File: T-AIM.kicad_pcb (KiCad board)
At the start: 2 copper layers, 44 parts, among them IC1 ATMEGA328PB-A, IC2 MAX17043, J1 ADXL345 Connector, J2 PIR Sensor Connector, J3 JY-MCU HC-05 Pins, SW1 Connection Button, SW2 Reset Button, U1 TPS61200

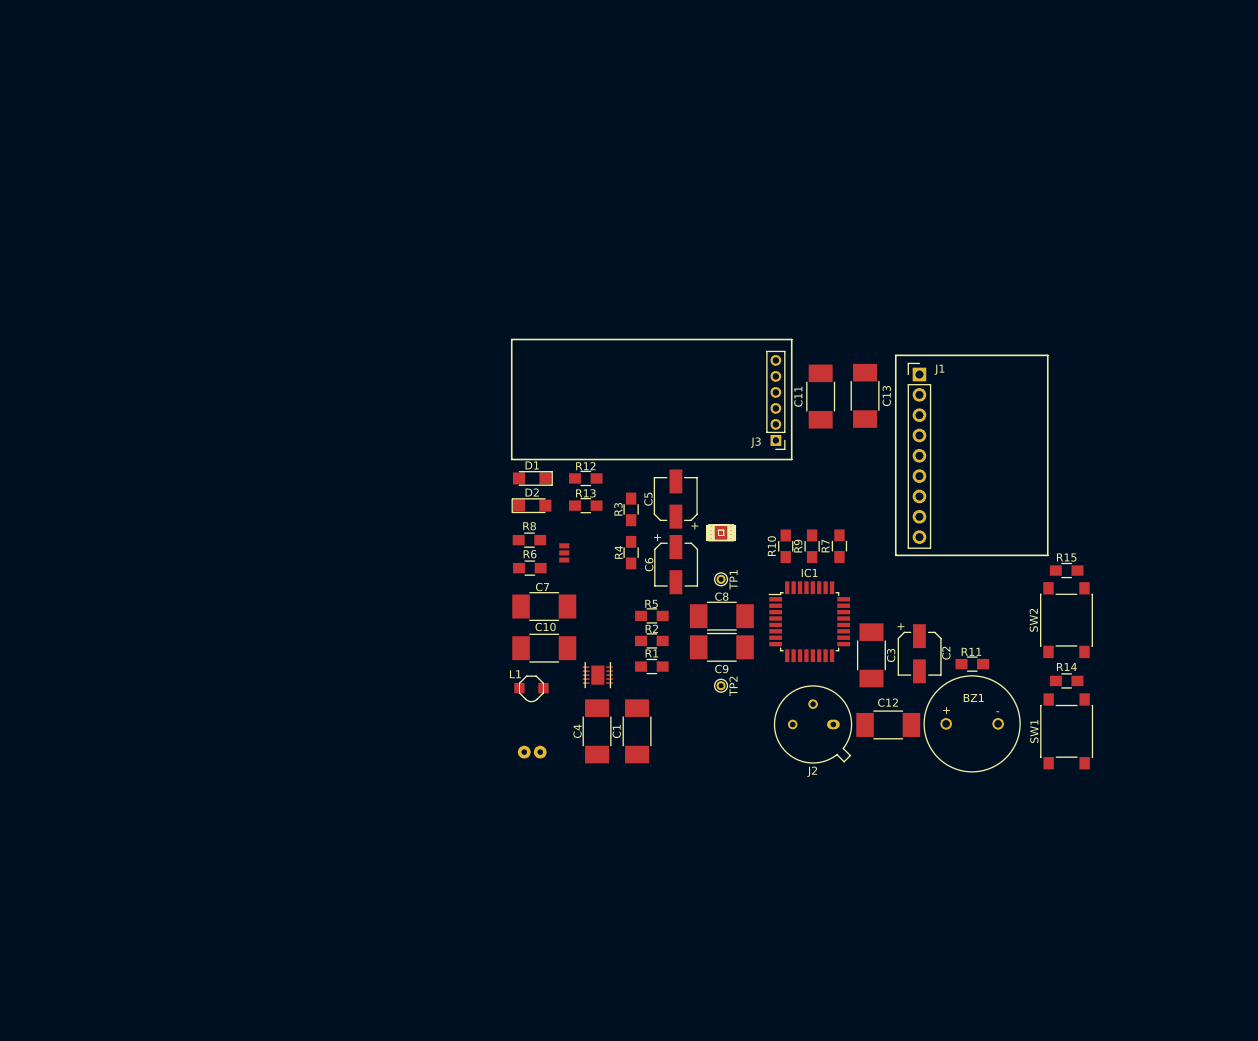
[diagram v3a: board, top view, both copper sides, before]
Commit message: First complete layout
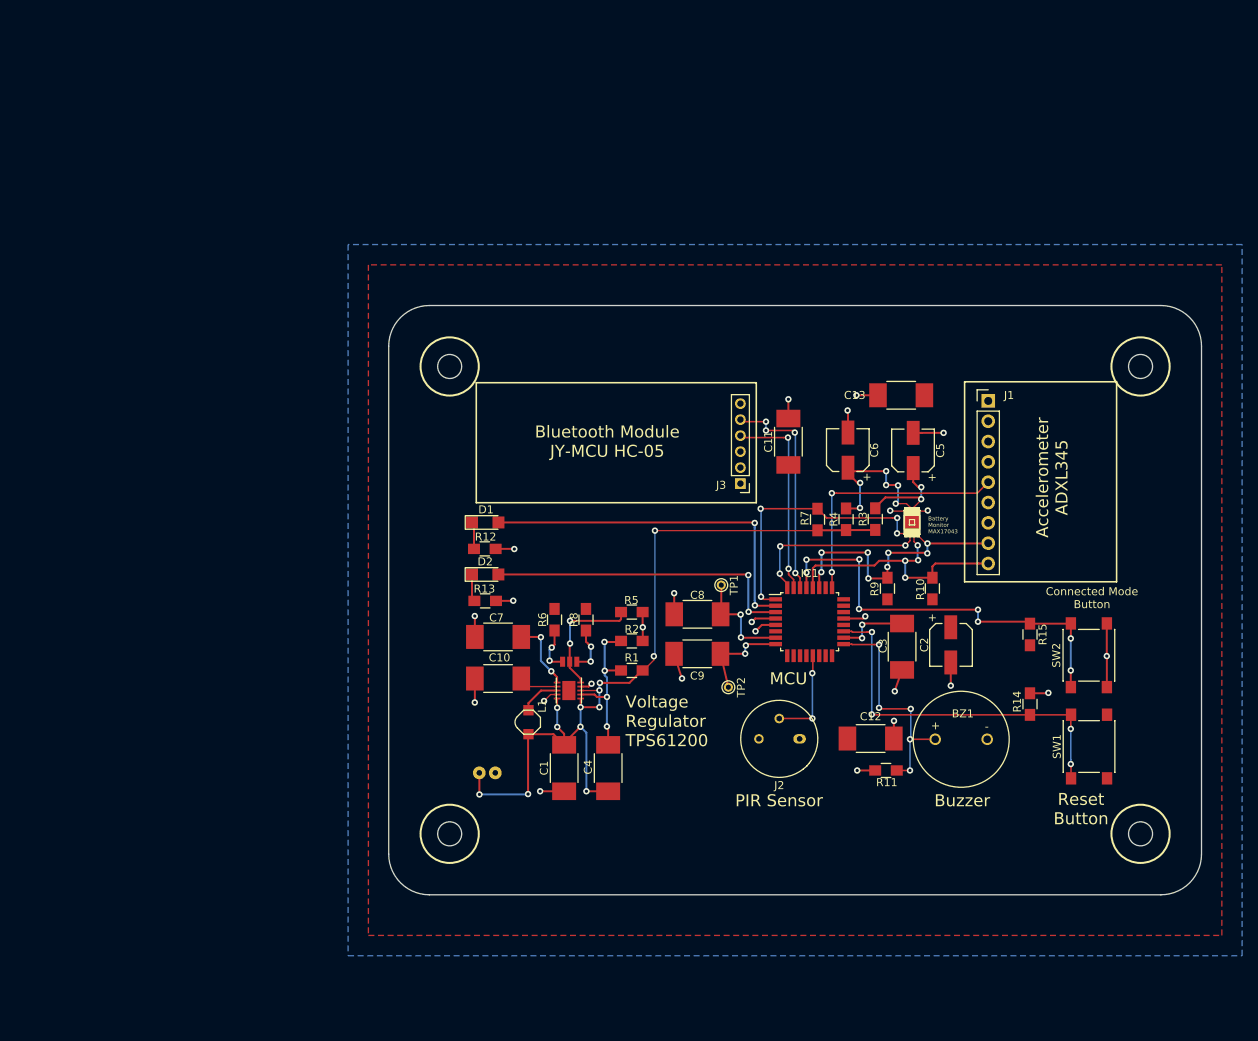
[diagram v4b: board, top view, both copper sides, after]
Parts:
- added ?: Screw_Hole_3_mm, T-AIM:Screw_Hole_3_mm, F.Cu at (118.9, 119.7)
- added ?: Screw_Hole_3_mm, T-AIM:Screw_Hole_3_mm, F.Cu at (205.3, 119.7)
- added ?: Screw_Hole_3_mm, T-AIM:Screw_Hole_3_mm, F.Cu at (205.3, 61.2)
- added ?: Screw_Hole_3_mm, T-AIM:Screw_Hole_3_mm, F.Cu at (118.9, 61.2)
- J2: footprint TO_SOT_Packages_THT:TO-5-3 -> T-AIM:TO-5-3
- moved R3 30.5 mm to (172.1, 80.3), turned to 90 degrees
- moved C5 30.3 mm to (176.8, 71.7)
- moved R4 27.2 mm to (168.5, 80.3), turned to 90 degrees
- moved C6 25.8 mm to (168.7, 71.7), turned to 90 degrees
- moved IC2 23.9 mm to (176.7, 80.7), turned to 270 degrees
- moved R10 19.1 mm to (179.2, 89.0)
- moved R13 17.3 mm to (123.3, 90.5)
- moved R11 17.1 mm to (173.4, 111.7), turned to 0 degrees
- moved R12 15.4 mm to (123.3, 84.0)
- moved SJ1 13.6 mm to (133.9, 98.2), turned to 0 degrees
- moved R8 12.2 mm to (135.9, 92.9), turned to 270 degrees
- moved R9 10.8 mm to (173.6, 89.0)
- moved D2 10.4 mm to (123.3, 87.2)
- moved C1 10.2 mm to (133.2, 111.4)
- moved R15 9.21 mm to (191.4, 94.7), turned to 90 degrees
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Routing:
- net VCC: track 0.00 -> 108.2 mm, vias 0 -> 12
- net GND: track 0.00 -> 67.2 mm, vias 0 -> 24
- net ResetButton: track 0.00 -> 52.5 mm, vias 0 -> 8
- net ConnectedButton: track 0.00 -> 46.8 mm, vias 0 -> 4
- net RedLED: track 0.00 -> 45.0 mm, vias 0 -> 2
- net BlueLED: track 0.00 -> 39.3 mm, vias 0 -> 2
- net /SDA: track 0.00 -> 34.8 mm, vias 0 -> 8
- net /SCL: track 0.00 -> 33.7 mm, vias 0 -> 4
- net BatteryLowAlert: track 0.00 -> 32.6 mm, vias 0 -> 4
- net INT1: track 0.00 -> 32.0 mm, vias 0 -> 2
- net AlarmBuzzer: track 0.00 -> 28.9 mm, vias 0 -> 5
- net BL_RXD: track 0.00 -> 27.8 mm, vias 0 -> 4
- net BL_TXD: track 0.00 -> 25.1 mm, vias 0 -> 2
- net FuelGaugeRestart: track 0.00 -> 23.0 mm, vias 0 -> 3
- net Net-(C6-Pad1): track 0.00 -> 21.3 mm, vias 0 -> 6
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- added copper zone on F.Cu, net 3V3
- added copper zone on B.Cu, net GND
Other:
- board outline added: 101.6 x 73.7 mm
- net class Power: clearance 0.2 -> 0.25; trace_width 0.2 -> 0.25
- net class Signal: clearance 0.1 -> 0.2; trace_width 0.1 -> 0.2
- board text added: "Accelerometer ADXL345"
- board text added: "Battery Monitor MAX17043"
- board text added: "Bluetooth Module JY-MCU HC-05"
- board text added: "Buzzer"
- board text added: "Connected Mode Button"
- board text added: "MCU"
- board text added: "PIR Sensor"
- board text added: "Reset Button"
- board text added: "Voltage Regulator TPS61200"

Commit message: Schematic updated for 3.7V; Changed Buzzer resistor to 1M; PCB updated for SF LiPo Gauge; Gerbers generated
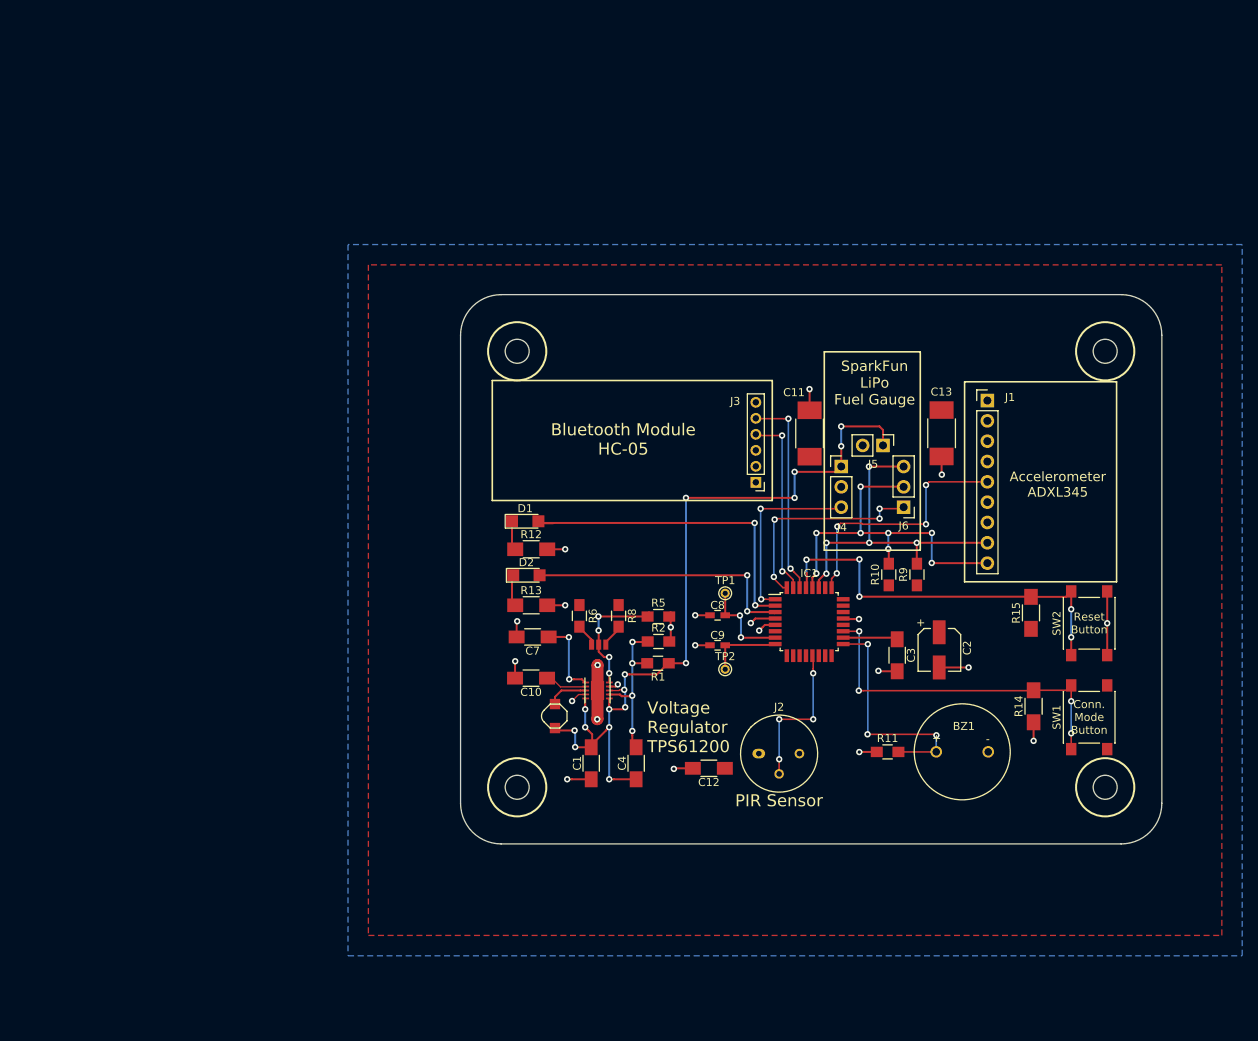
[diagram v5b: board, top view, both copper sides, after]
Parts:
- removed ? (x4): Screw_Hole_3_mm, T-AIM:Screw_Hole_3_mm
- removed C5: 1uF, Capacitors_SMD:CP_Elec_5x5.3
- removed C6: 10nF, Capacitors_SMD:CP_Elec_5x5.3
- removed IC2: MAX17043, SparkFun-PowerIC:TDFN-8
- removed JP1: M02JST-PTH-2, SparkFun-Connectors:JST-2-PTH
- removed R3: 1k, Resistors_SMD:R_0805_HandSoldering
- removed R4: 150, Resistors_SMD:R_0805_HandSoldering
- removed R7: 4.7k, Resistors_SMD:R_0805_HandSoldering
- added J4: CONN_01X03, Pin_Headers:Pin_Header_Straight_1x03_Pitch2.54mm, F.Cu at (167.9, 73.8)
- added J5: CONN_01X02, Pin_Headers:Pin_Header_Straight_1x02_Pitch2.54mm, F.Cu at (173.1, 71.1)
- added J6: CONN_01X03, Pin_Headers:Pin_Header_Straight_1x03_Pitch2.54mm, F.Cu at (175.7, 78.8)
- added S**: Screw_Hole_3_mm, T-AIM:Screw_Hole_3_mm, F.Cu at (127.3, 59.3)
- added S**: Screw_Hole_3_mm, T-AIM:Screw_Hole_3_mm, F.Cu at (200.8, 59.3)
- added S**: Screw_Hole_3_mm, T-AIM:Screw_Hole_3_mm, F.Cu at (200.8, 113.8)
- added S**: Screw_Hole_3_mm, T-AIM:Screw_Hole_3_mm, F.Cu at (127.3, 113.8)
- C1, C10, C12, C3, C4, C7: footprint Capacitors_SMD:C_1812_HandSoldering -> Capacitors_SMD:C_1206_HandSoldering
- C8, C9: footprint Capacitors_SMD:C_1812_HandSoldering -> Capacitors_SMD:C_0603_HandSoldering
- R12, R13, R14, R15: footprint Resistors_SMD:R_0805_HandSoldering -> Resistors_SMD:R_1206_HandSoldering
- R6: value 1.2M -> 1.37M
- moved C12 20.6 mm to (151.3, 111.5), turned to 180 degrees
- moved C13 6.93 mm to (180.4, 69.6), turned to 270 degrees
- moved R12 5.80 mm to (129.1, 84.1)
- moved R13 5.78 mm to (129.1, 91.1)
- moved R10 5.72 mm to (173.8, 87.3)
- moved J2 5.42 mm to (157.5, 109.6), turned to 0 degrees
- moved D2 5.15 mm to (128.5, 87.3)
- moved D1 5.00 mm to (128.3, 80.6)
- moved C7 4.32 mm to (129.3, 95.1)
- moved SJ1 4.21 mm to (137.5, 96.0)
- moved C10 4.12 mm to (129.1, 100.2)
- moved R8 4.10 mm to (140.0, 92.4)
- moved R9 4.08 mm to (177.3, 87.3)
- moved SW2 4.00 mm to (198.8, 93.3)
- moved SW1 3.66 mm to (198.8, 105.1)
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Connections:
- net /3.3V renamed /3.6V
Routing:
- net Net-(C6-Pad1): track 21.3 -> 0.00 mm, vias 6 -> 0
- net GND: track 67.2 -> 52.3 mm, vias 24 -> 20
- net /SCL: track 33.7 -> 47.3 mm, vias 4 -> 8
- net Net-(C5-Pad1): track 13.1 -> 0.00 mm, vias 2 -> 0
- net BatteryLowAlert: track 32.6 -> 23.3 mm, vias 4 -> 2
- net /SDA: track 34.8 -> 42.8 mm, vias 8 -> 5
- net PIR_OUT: track 12.0 -> 19.0 mm, vias 2 -> 4
- net (no net): track 0.00 -> 6.80 mm, vias 0 -> 2
- net VCC: track 108.2 -> 102.0 mm, vias 12 -> 16
- net BlueLED: track 39.3 -> 34.2 mm
- net FuelGaugeRestart: track 23.0 -> 27.5 mm, vias 3 -> 4
- net RedLED: track 45.0 -> 41.6 mm
- net /5V: track 5.90 -> 2.91 mm, vias 2 -> 0
- net Net-(C9-Pad1): track 12.2 -> 9.40 mm, vias 2 -> 0
- net BL_RXD: track 27.8 -> 25.5 mm, vias 4 -> 2
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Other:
- board size 101.6 x 73.7 mm -> 87.7 x 68.7 mm
- net class EP added: clearance 0.5, trace_width 0.5, via_dia 0.8, via_drill 0.4
- board text added: "Bluetooth Module HC-05"
- board text added: "Conn. Mode Button"
- board text added: "SparkFun LiPo Fuel Gauge"
- board text added: "T-AIM Sensor Board v0.1"
- board text added: "Tenager Mekonnen & Jani Väyrynen"
- board text removed: "Battery Monitor MAX17043"
- board text removed: "Bluetooth Module JY-MCU HC-05"
- board text removed: "Buzzer"
- board text removed: "Connected Mode Button"
- board text removed: "MCU"

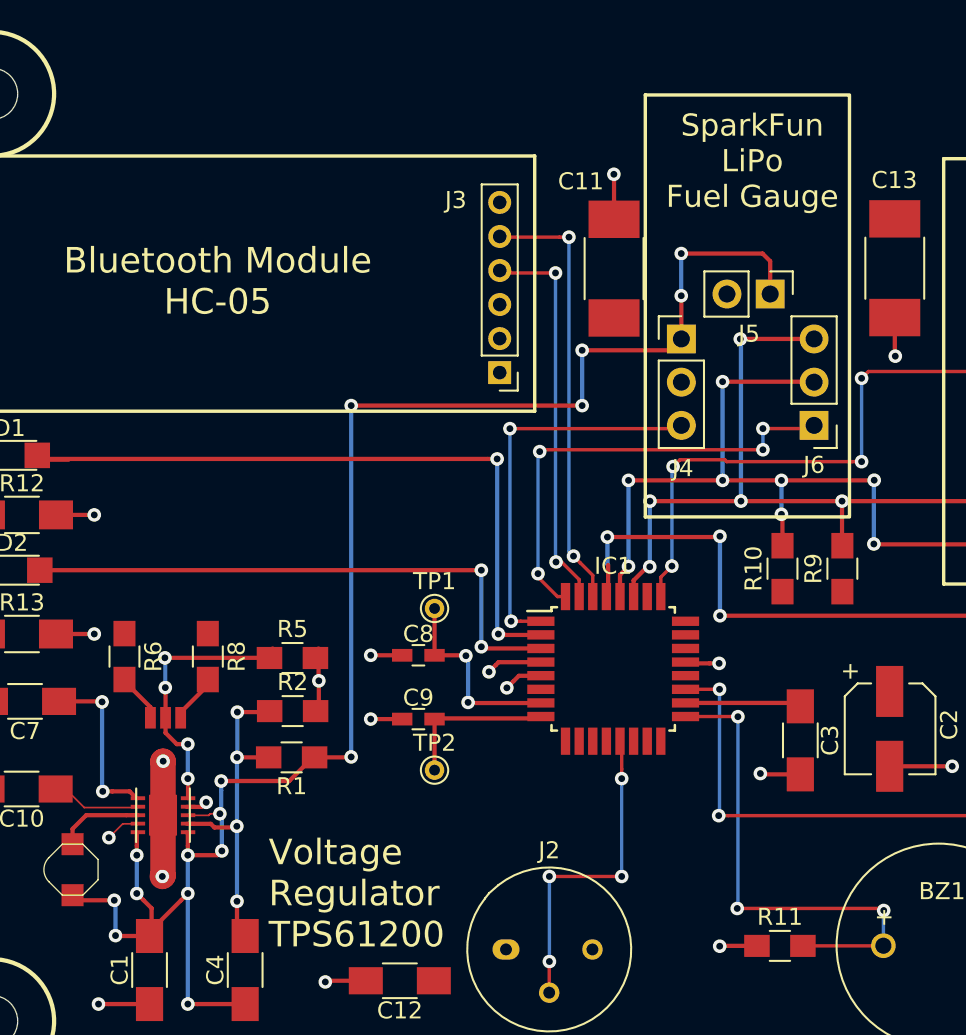
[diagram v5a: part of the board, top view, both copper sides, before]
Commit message: Updated TPS61200 Thermal Pad, PCB Layout and Gerbers; Slightly edited schematics
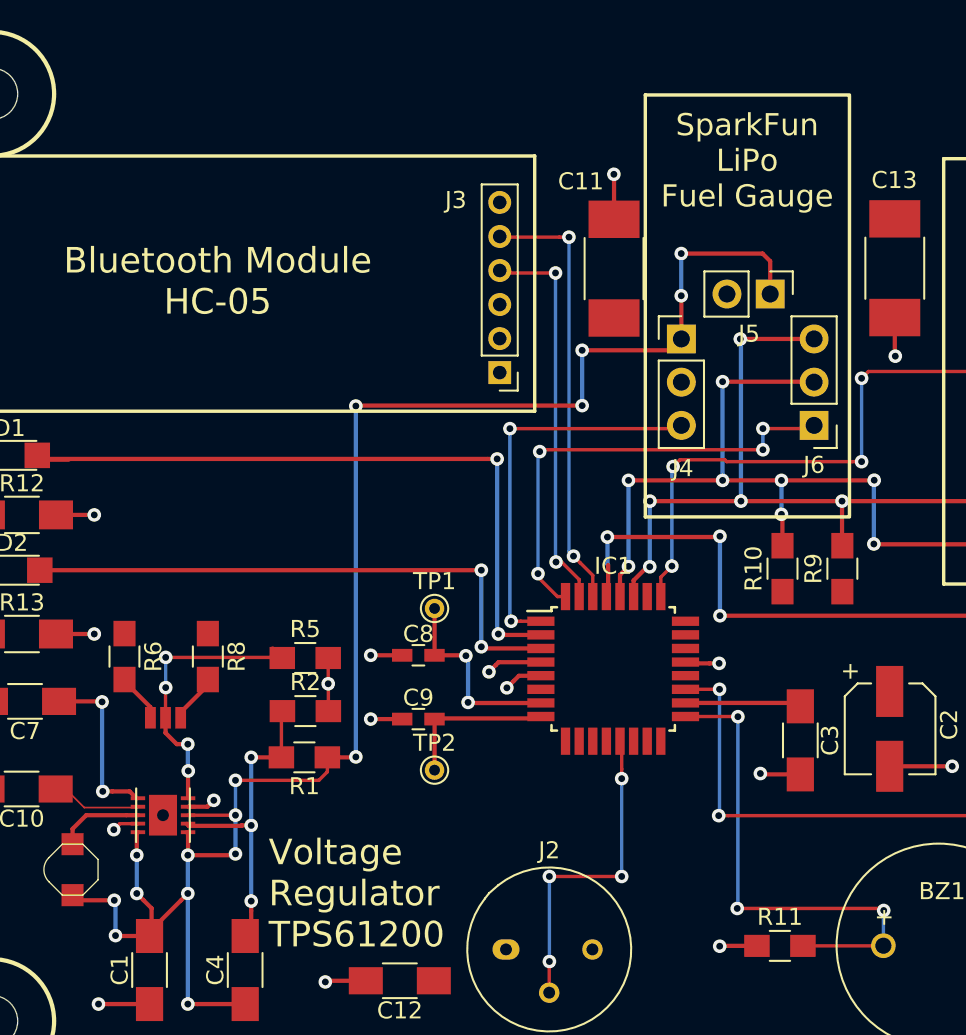
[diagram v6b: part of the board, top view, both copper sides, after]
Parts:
- R11: value 1k -> 1M
- U1: footprint SparkFun-PowerIC:DRC-10 -> DRC-10-Thermal-Vias
- moved R1 0.75 mm to (145.7, 98.3)
- moved R2 0.75 mm to (145.8, 95.6)
- moved R5 0.75 mm to (145.7, 92.5)
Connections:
- net 3V3 renamed 3V6
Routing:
- net (no net): track 6.80 -> 0.00 mm, vias 2 -> 0
- net Net-(C4-Pad2): track 20.1 -> 18.7 mm, vias 4 -> 3
- net VCC: track 102.0 -> 103.3 mm
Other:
- net class Default: clearance 0.25 -> 0.1
- net class EP: clearance 0.5 -> 0.25
- net class Power: clearance 0.25 -> 0.1
- net class Signal: clearance 0.2 -> 0.1
- rule trace_clearance: 0.25 -> 0.1
